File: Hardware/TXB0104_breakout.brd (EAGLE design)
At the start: 12.7 x 17.8 mm, 9 parts

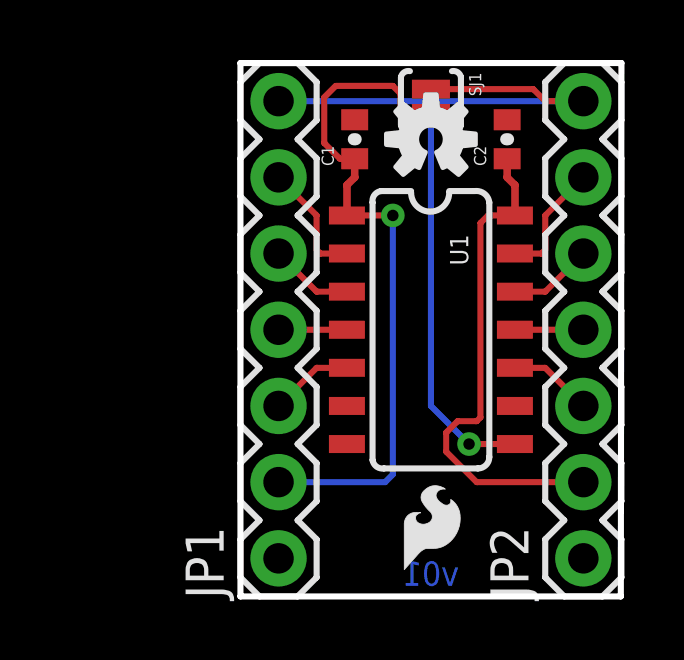
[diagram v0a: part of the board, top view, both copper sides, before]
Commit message: Changes for production  - Made vias .020"  - Fixed a couple of clearance errors  - Add silk for jumper on top  - Move C packages to true 0603  - Change version number
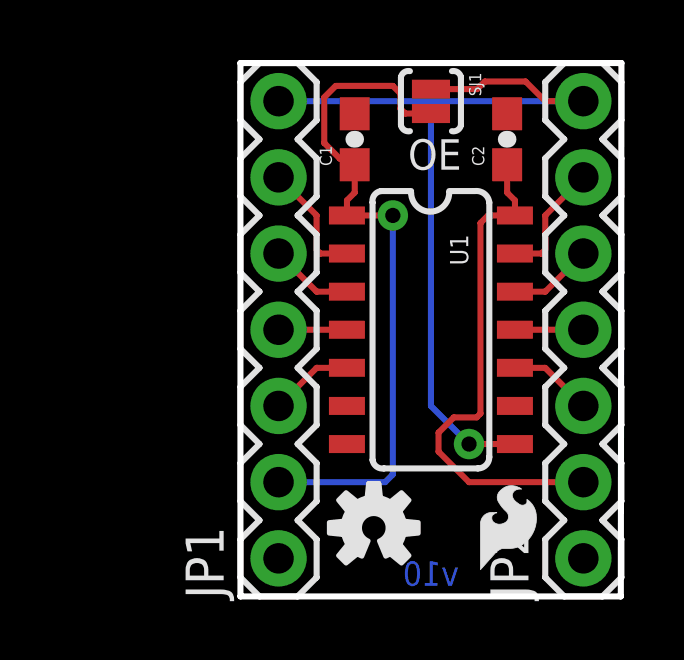
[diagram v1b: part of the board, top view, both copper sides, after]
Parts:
- C1, C2: device SparkFun-Capacitors:0402-CAP -> SparkFun-Capacitors:0603-CAP
- moved LOGO2 13.1 mm to (4.45, 2.29)
- moved LOGO1 2.54 mm to (8.00, 0.89)
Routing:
- net 5V: track 16.7 -> 17.4 mm
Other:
- board text added: "v10"
- board text removed: "v01"

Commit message: Production readied
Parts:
- added FID1, FID2: FIDUCIALUFIDUCIAL, SparkFun-Aesthetics:MICRO-FIDUCIAL
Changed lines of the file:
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@@
 <setting verticaltext="up"/>
 </settings>
-<grid distance="0.05" unitdist="inch" unit="inch" style="lines" multiple="1" display="yes" altdistance="0.005" altunitdist="inch" altunit="inch"/>
+<grid distance="0.001" unitdist="inch" unit="inch" style="lines" multiple="1" display="yes" altdistance="0.01" altunitdist="inch" altunit="inch"/>
 <layers>
 <layer number="1" name="Top" color="4" fill="1" visible="yes" active="yes"/>
-<layer number="2" name="Route2" color="1" fill="3" visible="no" active="yes"/>
-<layer number="15" name="Route15" color="4" fill="6" visible="no" active="yes"/>
+<layer number="2" name="Route2" color="1" fill="3" visible="yes" active="yes"/>
+<layer number="15" name="Route15" color="4" fill="6" visible="yes" active="yes"/>
 <layer number="16" name="Bottom" color="1" fill="1" visible="yes" active="yes"/>
 <layer number="17" name="Pads" color="2" fill="1" visible="yes" active="yes"/>
 <layer number="18" name="Vias" color="2" fill="1" visible="yes" active="yes"/>
 <layer number="19" name="Unrouted" color="6" fill="1" visible="yes" active="yes"/>
-<layer number="20" name="Dimension" color="15" fill="1" visible="yes" active="yes"/>
-<layer number="21" name="tPlace" color="16" fill="1" visible="yes" active="yes"/>
-<layer number="22" name="bPlace" color="14" fill="1" visible="yes" active="yes"/>
+<layer number="20" name="Dimension" color="6" fill="1" visible="yes" active="yes"/>
+<layer number="21" name="tPlace" color="6" fill="1" visible="yes" active="yes"/>
+<layer number="22" name="bPlace" color="6" fill="1" visible="yes" active="yes"/>
 <layer number="23" name="tOrigins" color="15" fill="1" visible="yes" active="yes"/>
 <layer number="24" name="bOrigins" color="15" fill="1" visible="yes" active="yes"/>
-<layer number="25" name="tNames" color="7" fill="1" visible="no" active="yes"/>
-<layer number="26" name="bNames" color="7" fill="1" visible="no" active="yes"/>
-<layer number="27" name="tValues" color="7" fill="1" visible="no" active="yes"/>
-<layer number="28" name="bValues" color="7" fill="1" visible="no" active="yes"/>
-<layer number="29" name="tStop" color="7" fill="3" visible="no" active="yes"/>
-<layer number="30" name="bStop" color="7" fill="6" visible="no" active="yes"/>
-<layer number="31" name="tCream" color="7" fill="4" visible="no" active="yes"/>
-<layer number="32" name="bCream" color="7" fill="5" visible="no" active="yes"/>
-<layer number="39" name="tKeepout" color="4" fill="11" visible="no" active="yes"/>
-<layer number="40" name="bKeepout" color="1" fill="11" visible="no" active="yes"/>
-<layer number="41" name="tRestrict" color="4" fill="10" visible="no" active="yes"/>
-<layer number="42" name="bRestrict" color="1" fill="10" visible="no" active="yes"/>
-<layer number="43" name="vRestrict" color="2" fill="10" visible="no" active="yes"/>
-<layer number="44" name="Drills" color="7" fill="1" visible="no" active="yes"/>
+<layer number="25" name="tNames" color="7" fill="1" visible="yes" active="yes"/>
+<layer number="26" name="bNames" color="7" fill="1" visible="yes" active="yes"/>
+<layer number="27" name="tValues" color="7" fill="1" visible="yes" active="yes"/>
+<layer number="28" name="bValues" color="7" fill="1" visible="yes" active="yes"/>
+<layer number="29" name="tStop" color="7" fill="3" visible="yes" active="yes"/>
+<layer number="30" name="bStop" color="7" fill="6" visible="yes" active="yes"/>
+<layer number="31" name="tCream" color="7" fill="4" visible="yes" active="yes"/>
+<layer number="32" name="bCream" color="7" fill="5" visible="yes" active="yes"/>
+<layer number="39" name="tKeepout" color="4" fill="11" visible="yes" active="yes"/>
+<layer number="40" name="bKeepout" color="1" fill="11" visible="yes" active="yes"/>
+<layer number="41" name="tRestrict" color="4" fill="10" visible="yes" active="yes"/>
+<layer number="42" name="bRestrict" color="1" fill="10" visible="yes" active="yes"/>
+<layer number="43" name="vRestrict" color="2" fill="10" visible="yes" active="yes"/>
+<layer number="44" name="Drills" color="7" fill="1" visible="yes" active="yes"/>
 <layer number="45" name="Holes" color="7" fill="1" visible="yes" active="yes"/>
-<layer number="46" name="Milling" color="3" fill="1" visible="no" active="yes"/>
+<layer number="46" name="Milling" color="3" fill="1" visible="yes" active="yes"/>
 <layer number="51" name="tDocu" color="6" fill="1" visible="yes" active="yes"/>
-<layer number="52" name="bDocu" color="7" fill="1" visible="no" active="yes"/>
+<layer number="52" name="bDocu" color="7" fill="1" visible="yes" active="yes"/>
 <layer number="3" name="Route3" color="4" fill="3" visible="no" active="no"/>
 <layer number="4" name="Route4" color="1" fill="4" visible="no" active="no"/>
@@
 <attribute name="PROD_ID" value="CAP-00810" x="33.02" y="34.29" size="1.778" layer="27" rot="R90" display="off"/>
 </element>
+<element name="FID1" library="SparkFun-Aesthetics" package="MICRO-FIDUCIAL" value="FIDUCIALUFIDUCIAL" x="7.62" y="14.3764"/>
+<element name="FID2" library="SparkFun-Aesthetics" package="MICRO-FIDUCIAL" value="FIDUCIALUFIDUCIAL" x="3.175" y="0.635"/>
 </elements>
 <signals>
@@
 </signal>
 </signals>
-<errors>
-</errors>
 </board>
 </drawing>
